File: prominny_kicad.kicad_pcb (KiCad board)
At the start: 2 copper layers, 136.2 x 92 mm, 21 parts, among them J1 Conn_01x03, SW1 SW_Push, SW2 SW_Push, SW3 SW_Push, SW4 SW_Push, SW5 SW_Push, SW6 SW_Push, SW7 SW_Push, U1 TRRS, U2 ProMicro

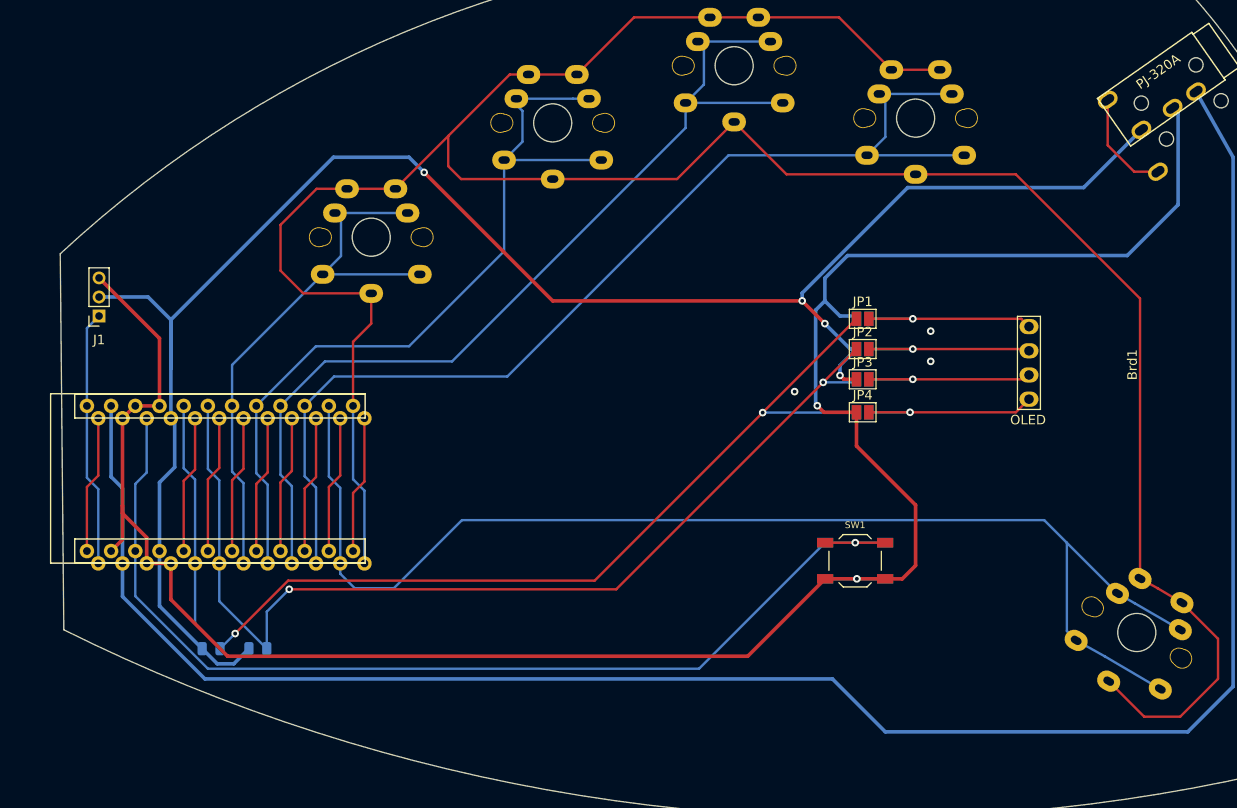
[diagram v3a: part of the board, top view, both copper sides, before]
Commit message: added silkscreen art, placed some traces new
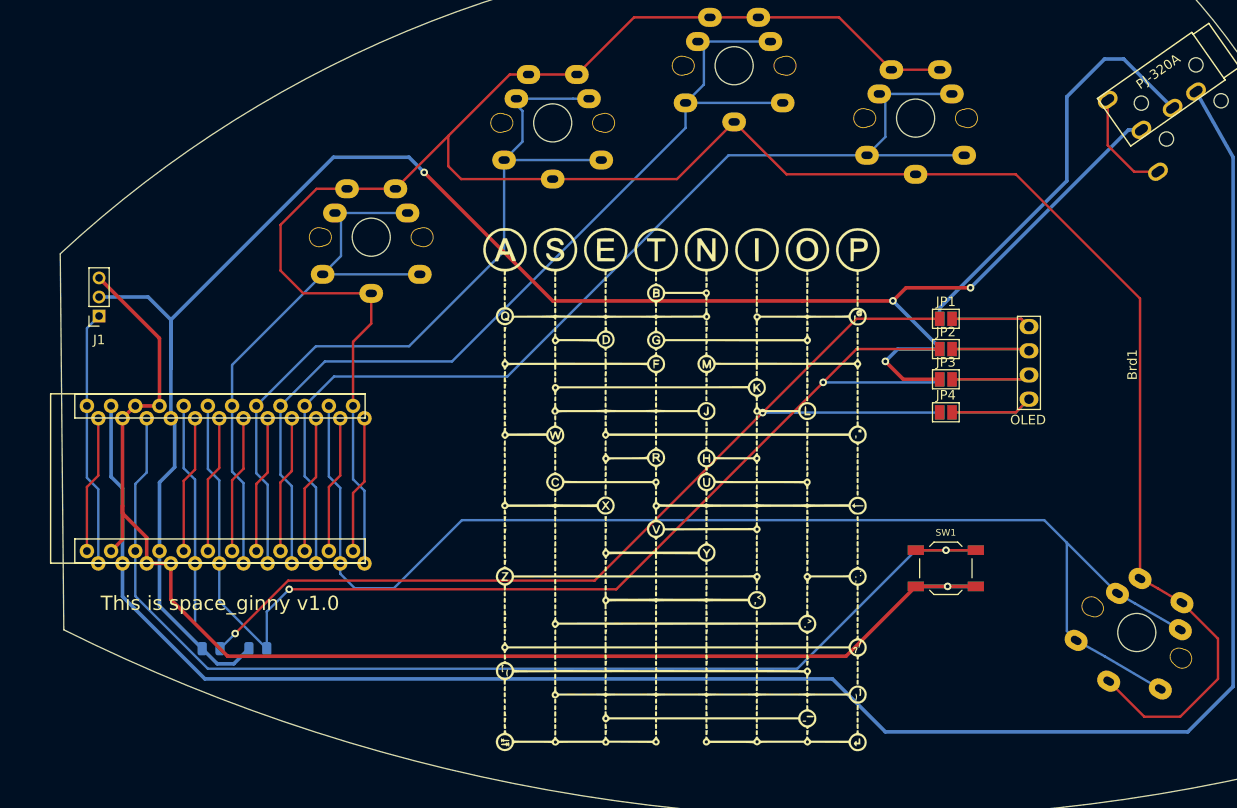
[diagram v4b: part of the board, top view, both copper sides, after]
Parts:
- added G***: LOGO, graphics:asetniop, F.Cu at (196.0, 109.5)
- moved SW1 9.56 mm to (223.8, 117.8)
- moved SW2 9.56 mm to (223.8, 117.8)
- moved JP1 8.73 mm to (223.8, 91.6)
- moved JP2 8.73 mm to (223.8, 94.7)
- moved JP3 8.73 mm to (223.8, 97.9)
- moved JP4 8.73 mm to (223.8, 101.4)
- moved JP5 8.73 mm to (223.8, 91.6)
- moved JP6 8.73 mm to (223.8, 94.7)
- moved JP7 8.73 mm to (223.8, 97.9)
- moved JP8 8.73 mm to (223.8, 101.4)
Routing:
- net ground: track 230.9 -> 188.4 mm, vias 5 -> 1
- net sda: track 118.1 -> 135.5 mm
- net scl: track 108.9 -> 126.3 mm
- net reset: track 112.8 -> 122.0 mm
- net power: track 193.4 -> 199.5 mm
- net Net-(Brd1-Pad3): track 21.5 -> 16.3 mm, vias 1 -> 0
- net Net-(Brd1-Pad2): track 21.6 -> 16.5 mm, vias 1 -> 0
- net Net-(Brd1-Pad4): track 21.8 -> 16.8 mm, vias 1 -> 0
- net Net-(Brd1-Pad1): track 21.7 -> 17.3 mm, vias 1 -> 0
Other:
- board text added: "This is space_ginny v1.0"

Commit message: changed mounting holes, added backside graphic
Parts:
- added  : MountingHole_2.2mm_M2_Pad_Via, MountingHole:MountingHole_2.2mm_M2_Pad_Via, F.Cu at (232.6, 134.1)
- added  : MountingHole_2.2mm_M2_Pad_Via, MountingHole:MountingHole_2.2mm_M2_Pad_Via, F.Cu at (234.9, 63.5)
- added  : MountingHole_2.2mm_M2_Pad_Via, MountingHole:MountingHole_2.2mm_M2_Pad_Via, F.Cu at (147.6, 88.9)
- added G***: LOGO, graphics:aset, B.Cu at (205.6, 100.0)
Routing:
- net power: track 199.5 -> 205.5 mm
- net ground: track 188.4 -> 192.3 mm, vias 1 -> 3
- net connection: track 208.4 -> 212.4 mm
